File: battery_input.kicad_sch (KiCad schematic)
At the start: 8 parts, among them J4 S2B-PH-SM4, U9 BQ27427

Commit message: finish all schematic changes
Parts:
- removed R17: 0R, Resistor_SMD:R_0402_1005Metric, symbol Device:R_Small
- added JP1: SolderJumper_2_Open, Jumper:SolderJumper-2_P1.3mm_Open_TrianglePad1.0x1.5mm, symbol Jumper:SolderJumper_2_Open
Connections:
- net ~{BATT_LOW}: now also JP1.2 (B)
- net at R16.1, U9.A1 (GPOUT): now also JP1.1 (A)
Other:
- moved on the sheet: C21, C23, R16, R19, U9

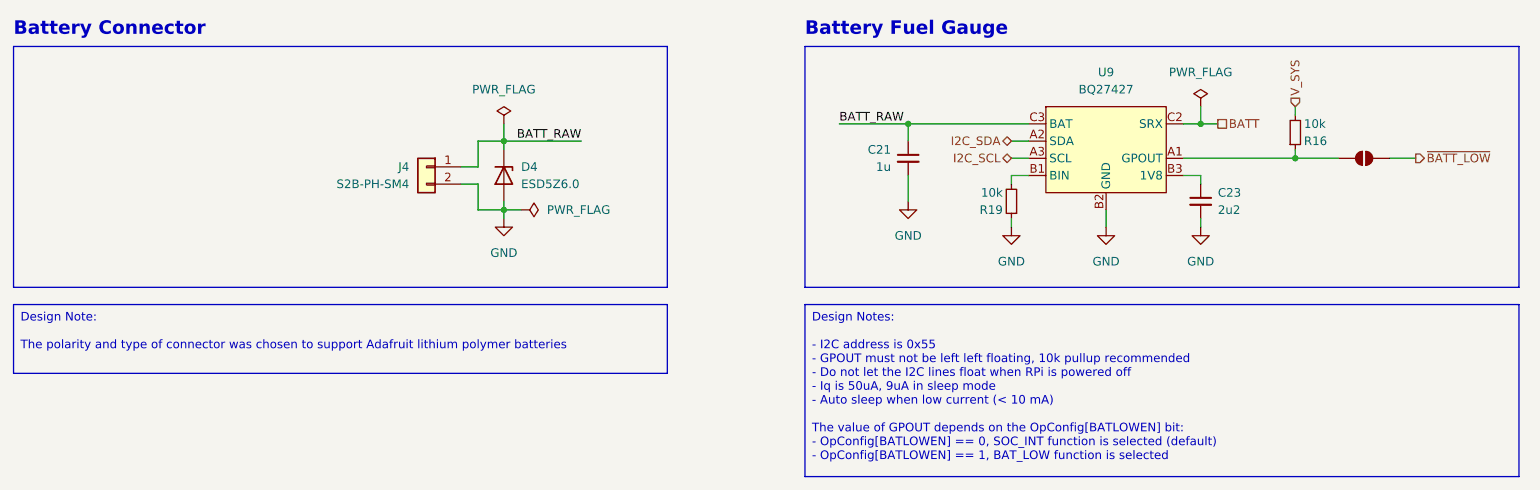
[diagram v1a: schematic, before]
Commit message: update to kicad 9.0
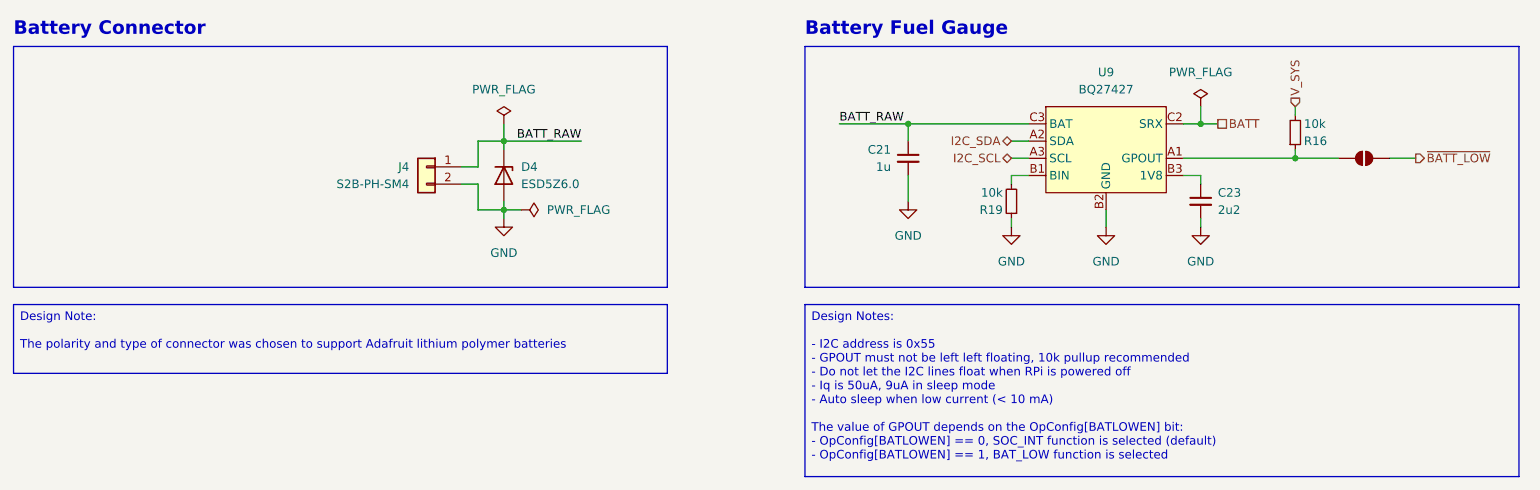
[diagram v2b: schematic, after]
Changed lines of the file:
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@@
 (kicad_sch
-	(version 20231120)
+	(version 20250114)
 	(generator "eeschema")
-	(generator_version "8.0")
+	(generator_version "9.0")
 	(paper "A4")
 	(title_block
@@
 		(comment 4 "Battery connector, ESD protection, and fuel gauge")
 	)
+	(rectangle
+		(start 38.1 57.15)
+		(end 134.62 92.71)
+		(stroke
+			(width 0)
+			(type default)
+		)
+		(fill
+			(type none)
+		)
+	)
+	(rectangle
+		(start 154.94 57.15)
+		(end 260.35 92.71)
+		(stroke
+			(width 0)
+			(type default)
+		)
+		(fill
+			(type none)
+		)
+	)
+	(text "Battery Connector"
+		(exclude_from_sim no)
+		(at 38.1 54.61 0)
+		(effects
+			(font
+				(size 2 2)
+				(thickness 0.4)
+				(bold yes)
+			)
+			(justify left)
+		)
+	)
+	(text "Battery Fuel Gauge"
+		(exclude_from_sim no)
+		(at 154.94 54.61 0)
+		(effects
+			(font
+				(size 2 2)
+				(thickness 0.4)
+				(bold yes)
+			)
+			(justify left)
+		)
+	)
+	(text_box "Design Note:\n\nThe polarity and type of connector was chosen to support Adafruit lithium polymer batteries"
+		(exclude_from_sim no)
+		(at 38.1 95.25 0)
+		(size 96.52 10.16)
+		(margins 0.9525 0.9525 0.9525 0.9525)
+		(stroke
+			(width 0)
+			(type default)
+		)
+		(fill
+			(type color)
+			(color 255 255 194 1)
+		)
+		(effects
+			(font
+				(size 1.27 1.27)
+				(thickness 0.1588)
+			)
+			(justify left top)
+		)
+	)
+	(text_box "Design Notes:\n\n- I2C address is 0x55\n- GPOUT must not be left left floating, 10k pullup recommended\n- Do not let the I2C lines float when RPi is powered off\n- Iq is 50uA, 9uA in sleep mode\n- Auto sleep when low current (< 10 mA)\n\nThe value of GPOUT depends on the OpConfig[BATLOWEN] bit:\n  - OpConfig[BATLOWEN] == 0, SOC_INT function is selected (default)\n  - OpConfig[BATLOWEN] == 1, BAT_LOW function is selected"
+		(exclude_from_sim no)
+		(at 154.94 95.25 0)
+		(size 105.41 25.4)
+		(margins 0.9525 0.9525 0.9525 0.9525)
+		(stroke
+			(width 0)
+			(type solid)
+		)
+		(fill
+			(type color)
+			(color 255 255 194 1)
+		)
+		(effects
+			(font
+				(size 1.27 1.27)
+				(thickness 0.1588)
+			)
+			(justify left top)
+		)
+	)
 	(junction
 		(at 110.49 71.12)
@@
 			(width 0)
 			(type default)
-		)
-	)
-	(rectangle
-		(start 38.1 57.15)
-		(end 134.62 92.71)
-		(stroke
-			(width 0)
-			(type default)
-		)
-		(fill
-			(type none)
-		)
-	)
-	(rectangle
-		(start 154.94 57.15)
-		(end 260.35 92.71)
-		(stroke
-			(width 0)
-			(type default)
-		)
-		(fill
-			(type none)
 		)
 	)
@@
 			"hoAlHU01+q/WnDqaa/VfrQAf8tPwqNf9aak/5afhUa/600AT0w/fFPph++KAGnoPqKd/y0/CmnoP"
 			"qKd/y0/CgBT3+lNP3x9P6049/pTT98fT+tACD79PP3x9DTB9+nn74+hoAdUEn3T/AJ71PUEn3T/n"
-			"vQBPRRRQB//Z"
-		)
-	)
-	(text_box "Design Note:\n\nThe polarity and type of connector was chosen to support Adafruit lithium polymer batteries"
-		(exclude_from_sim no)
-		(at 38.1 95.25 0)
-		(size 96.52 10.16)
-		(stroke
-			(width 0)
-			(type default)
-		)
-		(fill
-			(type color)
-			(color 255 255 194 1)
-		)
-		(effects
-			(font
-				(size 1.27 1.27)
-				(thickness 0.1588)
-			)
-			(justify left top)
-		)
-	)
-	(text_box "Design Notes:\n\n- I2C address is 0x55\n- GPOUT must not be left left floating, 10k pullup recommended\n- Do not let the I2C lines float when RPi is powered off\n- Iq is 50uA, 9uA in sleep mode\n- Auto sleep when low current (< 10 mA)\n\nThe value of GPOUT depends on the OpConfig[BATLOWEN] bit:\n  - OpConfig[BATLOWEN] == 0, SOC_INT function is selected (default)\n  - OpConfig[BATLOWEN] == 1, BAT_LOW function is selected"
-		(exclude_from_sim no)
-		(at 154.94 95.25 0)
-		(size 105.41 25.4)
-		(stroke
-			(width 0)
-			(type solid)
-		)
-		(fill
-			(type color)
-			(color 255 255 194 1)
-		)
-		(effects
-			(font
-				(size 1.27 1.27)
-				(thickness 0.1588)
-			)
-			(justify left top)
-		)
-	)
-	(text "Battery Connector"
-		(exclude_from_sim no)
-		(at 38.1 54.61 0)
-		(effects
-			(font
-				(size 2 2)
-				(thickness 0.4)
-				(bold yes)
-			)
-			(justify left)
-		)
-	)
-	(text "Battery Fuel Gauge"
-		(exclude_from_sim no)
-		(at 154.94 54.61 0)
-		(effects
-			(font
-				(size 2 2)
-				(thickness 0.4)
-				(bold yes)
-			)
-			(justify left)
+			"vQBPRRRQB//ZMjMuemlwAIA/AAAAAAAAgD8AAAAAAACAPwAAAAAAAIA/AAAAAAAAgD8AAAAAAACA"
+			"PwAAAAAAAAAAVgAAAAAAgD8AAAAAAAAAAFYAAAAAAIA/AAAAAAAAgD8CAAAAAQAAACAAAAAAAAAA"
+			"AAAAAAAAAAAAAgAAAAAAAMAAAAAAAAAAINMyhth/AAAAAKJEAAAwxAAAgD8AAKJEAAAwRAAAAAAA"
+			"AAAAAAAAAGXgU8G+hEBBo0u8wYzut0EAAAAAAAAiRQAAAAAAALBEAACiRAAAMMQAAIA/AACiRAAA"
+			"MEQAAAAAAAAAAAAAAABl4FPBvoRAQaNLvMGM7rdBAAAAAAAAIkUAAAAAAACwRAAAokQAADDEAACA"
+			"PwAAokQAADBEAAAAAAAAAAAAAAAAZeBTwb6EQEGjS7zBjO63QQAAAAAAACJFAAAAAAAAsEQAAKJE"
+			"AAAwxAAAgD8AAKJEAAAwRAAAAAAAAAAAAAAAAGXgU8G+hEBBo0u8wYzut0EAAAAAAAAiRQAAAAAA"
+			"ALBEAACiRAAAMMQAAIA/AACiRAAAMEQAAAAAAAAAAAAAAABl4FPBvoRAQaNLvMGM7rdBAAAAAAAA"
+			"IkUAAAAAAACwRAAAokQAADDEAACAPwAAokQAADBEAAAAAAAAAAAAAAAAZeBTwb6EQEGjS7zBjO63"
+			"QQAAAAAAACJFAAAAAAAAsEQAAKJEAAAwxAAAgD8AAKJEAAAwRAAAAAAAAAAAAAAAAGXgU8G+hEBB"
+			"o0u8wYzut0EAAAAAAAAiRQAAAAAAALBEAACiRAAAMMQAAIA/AACiRAAAMEQAAAAAAAAAAAAAAABl"
+			"4FPBvoRAQaNLvMGM7rdBAAAAAAAAIkUAAAAAAACwRAAAokQAADDEAACAPwAAokQAADBEAAAAAAAA"
+			"AAAAAAAAZeBTwb6EQEGjS7zBjO63QQAAAAAAACJFAAAAAAAAsEQAAKJEAAAwxAAAgD8AAKJEAAAw"
+			"RAAAAAAAAAAAAAAAAGXgU8G+hEBBo0u8wYzut0EAAAAAAAAiRQAAAAAAALBEAACiRAAAMMQAAIA/"
+			"AACiRAAAMEQAAAAAAAAAAAAAAABl4FPBvoRAQaNLvMGM7rdBAAAAAAAAIkUAAAAAAACwRAAAokQA"
+			"ADDEAACAPwAAokQAADBEAAAAAAAAAAAAAAAAZeBTwb6EQEGjS7zBjO63QQAAAAAAACJFAAAAAAAA"
+			"sEQAAKJEAAAwxAAAgD8AAKJEAAAwRAAAAAAAAAAAAAAAAGXgU8G+hEBBo0u8wYzut0EAAAAAAAAi"
+			"RQAAAAAAALBEAACiRAAAMMQAAIA/AACiRAAAMEQAAAAAAAAAAAAAAABl4FPBvoRAQaNLvMGM7rdB"
+			"AAAAAAAAIr/VfxHkDr+mvwAAAAAAAAAACQnSTvf/779y99wqlHRnv0MOLkkr0jM/0dnRTvf/77/0"
+			"1NxqlHRnvxPxLWkr0jM/hfJJq+8877/ZwgjqKcTLv4XAeiqY/xy/M0R+2EFU77+wt8AZhhLKv1de"
+			"PjogBjg/pMG3Zen377/VfxHkDr+mvwAAAAAAAAAAhfJJq+8877/ZwgjqKcTLv4XAeiqY/xy/Oa3S"
+			"Tvf/779jb91Kk3Rnv/ZzLkkr0jM/oM6RkNh/AAAQAAAAAAAAAAAAAAAAAAAAAQAAAAEHAAADAAAA"
+			"AgAAAKAdkZDYfwAAAAAAAAAAAAAAAAAAAAAAAAAAAAAAAAAACAAAAAEHAAUAAAAAAgAAAMgdkZDY"
+			"fwAAQQAEAAIAAAAAAAAAAAAAAAAAAAAAAAAACAAAAAEKAgUAAAAAAwAAAAAAAAAAAAAADwAAAAMA"
+			"AAABAAAAAAAAAGDmoB8AYAAAYOagHwBgAABo5qAfAGAAAAEdkZDYfwAAaM+RkNh/AABoz5GQ2H8A"
+			"ABAAAAAAAAAAAAAAAAEHAAUAAAAABAAAABgekZDYfwAAEAAAAAQAAAAAAAAAAAAAAAAAAAAAAAAA"
+			"CAAAAAEKAgUAAAAABAAAAAAAAAAAAAAAZQEEAAQAAAAAAAAAAAAAAAAAAAAAAAAAAQAAAAEHAAAD"
+			"AAAABQAAAEAekZDYfwAAAAAAAAAAAAAAAAAAAAAAAAMAAAAAAAAA0M6gHwBgAADQzqAfAGAAANjO"
+			"oB8AYAAAAEAAAAYAAAAw0JGQ2H8AADDQkZDYfwAAEAAAAAAAAAAAAAAABgAAAGgekZDYfwAAAAAA"
+			"AAAAAAAAAAAAAAAAAAAAAAAAAAAACAAAAAEHAAUAQAAABwAAAAAAAAAAAAAASAAAAAcAAAAAAAAA"
+			"AAAAAAAAAAAAAAAAAQAAAAEHAACDAQAABwAAAJAekZDYfwAAAAAAAAAAAAAAAAAAAAAAAAAAAAAA"
+			"AAAAAQAAAAEHAAVw0KAfAGAAAHDQoB8AYAAAeNCgHwBgAAAAAAAAAAAAAPjQkZDYfwAA+NCRkNh/"
+			"AAAQAAAAAAAAAAAAAADYfwAAAAAAAAAAAAAAAAAAAAAAAAAAAAAAAAAACAAAAAEHAAUAAgAACQAA"
+			"AOAekZDYfwAAAAAAAAAAAAAAAAAAAAAAAAAAAAAAAAAACAAAAAEHAAUAQAAACgAAAAgfkZDYfwAA"
+			"AAAAAAAAAAAAAAAAAAAAAAAAAAAAAAAACAAAAAEHAAUBAAAACgAAANDUoB8AYAAA0NSgHwBgAADY"
+			"1KAfAGAAAAEAAAAAAAAACAAAAAEHAAUAAwAACwAAAFgfkZDYfwAAAAAAAAAAAAAAAAAAAAAAAAAA"
+			"AAAAAAAACA=="
 		)
 	)
 	(label "BATT_RAW"
 		(at 160.02 68.58 0)
-		(fields_autoplaced yes)
 		(effects
 			(font
@@
 	(label "BATT_RAW"
 		(at 121.92 71.12 180)
-		(fields_autoplaced yes)
 		(effects
 			(font
@@
 		(shape passive)
 		(at 215.9 68.58 0)
-		(fields_autoplaced yes)
 		(effects
 			(font
@@
 		(shape output)
 		(at 245.11 73.66 0)
-		(fields_autoplaced yes)
 		(effects
 			(font
@@
 		(shape input)
 		(at 227.33 66.04 90)
-		(fields_autoplaced yes)
 		(effects
 			(font
@@
 		(shape bidirectional)
 		(at 185.42 71.12 180)
-		(fields_autoplaced yes)
 		(effects
 			(font
@@
 		(shape bidirectional)
 		(at 185.42 73.66 180)
-		(fields_autoplaced yes)
 		(effects
 			(font

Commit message: add jobset file, update outputs
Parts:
- U9: footprint Package_BGA:Texas_DSBGA-9_1.62mmx1.58mm_Layout3x3_P0.5mm -> Package_BGA:Texas_DSBGA-9_1.62x1.58mm_Layout3x3_P0.5mm
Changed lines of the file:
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@@
 			"AAAAAAAAAAAAAAAAAAAAAAAAAAAAAAAACAAAAAEHAAUBAAAACgAAANDUoB8AYAAA0NSgHwBgAADY"
 			"1KAfAGAAAAEAAAAAAAAACAAAAAEHAAUAAwAACwAAAFgfkZDYfwAAAAAAAAAAAAAAAAAAAAAAAAAA"
-			"AAAAAAAACA=="
+			"AAAAAAAACICAgICAgICAgICAgICAgICAgICAgICAgICAgICAgICAgICAgICAgICAgICAgICAgICA"
+			"gICAgICAgICAgICAgICAgICAgICAgICAgICAgICAgICAgICAgICAgICAgICAgICAgICAgICAgICA"
+			"gICAgICAgICAgICAgICAgICAgICAgICAgICAgICAgICAgICAgICAgICAgICAgICAgICAgICAgICA"
+			"gICAgICAgICAgICAgICAgICAgICAgICAgICAgICAgICAgICAgICAgICAgICAgICAgICAgICAgICA"
+			"gICAgICAgICAgICAgICAgICAgICAgICAgICAgICAgICAgICAgICAgICAgICAgICAgICAgICAgICA"
+			"gICAgICAgICAgICAgICAgICAgICAgICAgICAgICAgICAgICAgICAgICAgICAgICAgICAgICAgICA"
+			"gICAgICAgICAgICAgICAgICAgICAgICAgICAgICAgICAgICAgICAgICAgICAgICAgICAgICAgICA"
+			"gICAgICAgICAgICAgICAgICAgICAgICAgICAgICAgICAgICAgICAgICAgICAgICAgICAgICAgICA"
+			"gICAgICAgICAgICAgICAgICAgICAgICAgICAgICAgICAgICAgICAgICAgICAgICAgICAgICAgICA"
+			"gICAgICAgICAgICAgICAgICAgICAgICAgICAgICAgICAgICAgICAgICAgICAgICAgICAgICAgICA"
+			"gICAgICAgICAgICAgICAgICAgICAgICAgICAgICAgICAgICAgICAgICAgICAgICAgICAgICAgICA"
+			"gICAgICAgICAgICAgICAgICAgICAgICAgICAgICAgICAgICAgICAgICAgICAgICAgICAgICAgICA"
+			"gICAgICAgICAgICAgICAgICAgICAgICAgICAgICAgICAgICAgICAgICAgICAgICAgICAgICAgICA"
+			"gICAgICAgICAgICAgICAgICAgICAgICAgICAgICAgICAgICAgICAgICAgICAgICAgICAgICAgICA"
+			"gICAgICAgICAgICAgICAgICAgICAgICAgICAgICAgICAgICAgICAgICAgICAgICAgICAgICAgICA"
+			"gICAgICAgICAgICAgICAgICAgICAgICAgICAgICAgICAgICAgICAgICAgICAgICAgICAgICAgICA"
+			"gICAgICAgICAgICAgICAgICAgICAgICAgICAgICAgICAgICAgICAgICAgICAgICAgICAgICAgICA"
+			"gICAgICAgICAgICAgICAgICAgICAgICAgICAgICAgICAgICAgICAgICAgICAgICAgICAgICAgICA"
+			"gICAgICAgA=="
 		)
 	)
@@
 			)
 		)
-		(property "Footprint" "Package_BGA:Texas_DSBGA-9_1.62mmx1.58mm_Layout3x3_P0.5mm"
+		(property "Footprint" "Package_BGA:Texas_DSBGA-9_1.62x1.58mm_Layout3x3_P0.5mm"
 			(at 199.39 72.39 0)
 			(effects
